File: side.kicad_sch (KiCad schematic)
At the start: 52 parts, among them SW1 SW_Push, SW11 SW_Push, SW12 SW_Push, SW13 SW_Push, SW14 SW_Push, SW15 SW_Push, SW21 SW_Push, SW22 SW_Push, SW23 SW_Push, SW24 SW_Push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

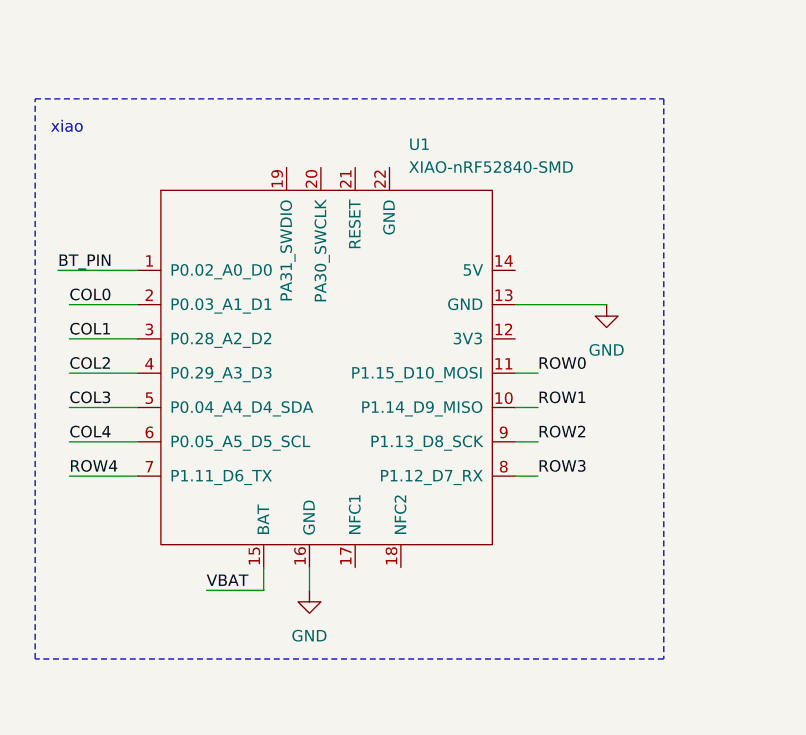
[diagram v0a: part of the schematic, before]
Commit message: Added links to parts
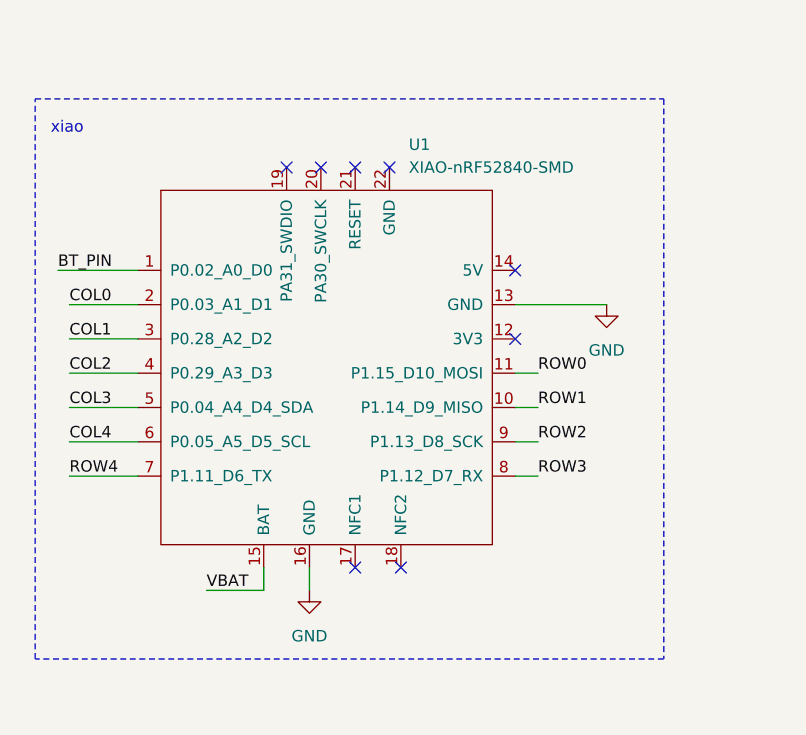
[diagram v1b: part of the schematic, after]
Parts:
- D1, D11, D12, D13, D14, D15, D21, D22, D23, D24, D25, D3, D31, D32, D33, D34, D35, D41, D5, D7, D9: footprint (none) -> Diode_SMD:D_SOD-123
- H1, H3, H5, H6, H9: footprint (none) -> Panelization:mouse-bite-5mm-slot
- R1, R3: footprint (none) -> Resistor_SMD:R_0805_2012Metric
- SW1, SW11, SW12, SW13, SW14, SW15, SW21, SW22, SW23, SW24, SW25, SW3, SW31, SW32, SW33, SW34, SW35, SW41, SW5, SW7, SW9: footprint (none) -> PCM_marbastlib-choc:SW_choc_v1_HS_CPG135001S30_1u
- TP1, TP3: footprint (none) -> TestPoint:TestPoint_Pad_D2.0mm
- U1: footprint (none) -> XIAO:modified-XIAO-nRF52840-SMD
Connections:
- no-connect marks 0 -> 8
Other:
- title: (none) -> Keyboard
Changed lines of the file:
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@@
 	(generator_version "9.0")
 	(paper "A4")
+	(title_block
+		(title "Keyboard")
+		(date "2026-04-17")
+		(comment 1 "Keyboard Schematic Editor")
+	)
 	(rectangle
 		(start 31.75 78.74)
@@
 		(color 0 0 0 0)
 	)
+	(no_connect
+		(at 67.31 86.36)
+	)
+	(no_connect
+		(at 85.09 105.41)
+	)
+	(no_connect
+		(at 85.09 97.79)
+	)
+	(no_connect
+		(at 63.5 86.36)
+	)
+	(no_connect
+		(at 59.69 86.36)
+	)
+	(no_connect
+		(at 67.31 130.81)
+	)
+	(no_connect
+		(at 72.39 130.81)
+	)
+	(no_connect
+		(at 71.12 86.36)
+	)
 	(wire
 		(pts
@@
 	(wire
 		(pts
+			(xy 85.09 101.6) (xy 95.25 101.6)
+		)
+		(stroke
+			(width 0)
+			(type default)
+		)
+	)
+	(wire
+		(pts
 			(xy 34.29 97.79) (xy 43.18 97.79)
 		)
@@
 	(wire
 		(pts
-			(xy 85.09 101.6) (xy 95.25 101.6)
-		)
-		(stroke
-			(width 0)
-			(type default)
-		)
-	)
-	(wire
-		(pts
 			(xy 234.95 97.79) (xy 234.95 115.57)
 		)
@@
 			)
 		)
-		(property "Footprint" ""
+		(property "Footprint" "PCM_marbastlib-choc:SW_choc_v1_HS_CPG135001S30_1u"
 			(at 207.01 110.49 0)
 			(effects
@@
 			)
 		)
-		(property "Footprint" ""
+		(property "Footprint" "PCM_marbastlib-choc:SW_choc_v1_HS_CPG135001S30_1u"
 			(at 223.52 110.49 0)
 			(effects
@@
 			)
 		)
-		(property "Footprint" ""
+		(property "Footprint" "PCM_marbastlib-choc:SW_choc_v1_HS_CPG135001S30_1u"
 			(at 173.99 74.93 0)
 			(effects
@@
 			)
 		)
-		(property "Footprint" ""
+		(property "Footprint" "Diode_SMD:D_SOD-123"
 			(at 195.58 119.38 0)
 			(effects
@@
 			)
 		)
-		(property "Footprint" ""
+		(property "Footprint" "PCM_marbastlib-choc:SW_choc_v1_HS_CPG135001S30_1u"
 			(at 207.01 57.15 0)
 			(effects
@@
 			)
 		)
-		(property "Footprint" ""
+		(property "Footprint" "PCM_marbastlib-choc:SW_choc_v1_HS_CPG135001S30_1u"
 			(at 240.03 74.93 0)
 			(effects
@@
 			)
 		)
-		(property "Footprint" ""
+		(property "Footprint" "PCM_marbastlib-choc:SW_choc_v1_HS_CPG135001S30_1u"
 			(at 223.52 57.15 0)
 			(effects
@@
 			)
 		)
-		(property "Footprint" ""
+		(property "Footprint" "PCM_marbastlib-choc:SW_choc_v1_HS_CPG135001S30_1u"
 			(at 223.52 92.71 0)
 			(effects
@@
 			)
 		)
-		(property "Footprint" ""
+		(property "Footprint" "Panelization:mouse-bite-5mm-slot"
 			(at 44.45 186.69 0)
 			(effects
@@
 			)
 		)
-		(property "Footprint" ""
+		(property "Footprint" "Diode_SMD:D_SOD-123"
 			(at 195.58 101.6 0)
 			(effects
@@
 			)
 		)
-		(property "Footprint" ""
+		(property "Footprint" "PCM_marbastlib-choc:SW_choc_v1_HS_CPG135001S30_1u"
 			(at 190.5 92.71 0)
 			(effects
@@
 			)
 		)
-		(property "Footprint" ""
+		(property "Footprint" "Diode_SMD:D_SOD-123"
 			(at 212.09 66.04 0)
 			(effects
@@
 			)
 		)
-		(property "Footprint" ""
+		(property "Footprint" "PCM_marbastlib-choc:SW_choc_v1_HS_CPG135001S30_1u"
 			(at 240.03 110.49 0)
 			(effects
@@
 			)
 		)
-		(property "Footprint" ""
+		(property "Footprint" "PCM_marbastlib-choc:SW_choc_v1_HS_CPG135001S30_1u"
 			(at 173.99 57.15 0)
 			(effects
@@
 			)
 		)
-		(property "Footprint" ""
+		(property "Footprint" "PCM_marbastlib-choc:SW_choc_v1_HS_CPG135001S30_1u"
 			(at 240.03 57.15 0)
 			(effects
@@
 			)
 		)
-		(property "Footprint" ""
+		(property "Footprint" "PCM_marbastlib-choc:SW_choc_v1_HS_CPG135001S30_1u"
 			(at 207.01 74.93 0)
 			(effects
@@
 			)
 		)
-		(property "Footprint" ""
+		(property "Footprint" "Resistor_SMD:R_0805_2012Metric"
 			(at 82.55 44.958 90)
 			(effects
@@
 			)
 		)
-		(property "Footprint" ""
+		(property "Footprint" "Diode_SMD:D_SOD-123"
 			(at 245.11 83.82 0)
 			(effects
@@
 			)
 		)
-		(property "Footprint" ""
+		(property "Footprint" "PCM_marbastlib-choc:SW_choc_v1_HS_CPG135001S30_1u"
 			(at 173.99 92.71 0)
 			(effects
@@
 			)
 		)
-		(property "Footprint" ""
+		(property "Footprint" "Diode_SMD:D_SOD-123"
 			(at 228.6 66.04 0)
 			(effects
@@
 			)
 		)
-		(property "Footprint" ""
+		(property "Footprint" "Diode_SMD:D_SOD-123"
 			(at 179.07 66.04 0)
 			(effects
@@
 			)
 		)
-		(property "Footprint" ""
+		(property "Footprint" "Diode_SMD:D_SOD-123"
 			(at 212.09 83.82 0)
 			(effects
@@
 			)
 		)
-		(property "Footprint" ""
+		(property "Footprint" "PCM_marbastlib-choc:SW_choc_v1_HS_CPG135001S30_1u"
 			(at 207.01 92.71 0)
 			(effects
@@
 			)
 		)
-		(property "Footprint" ""
+		(property "Footprint" "PCM_marbastlib-choc:SW_choc_v1_HS_CPG135001S30_1u"
 			(at 190.5 110.49 0)
 			(effects
@@
 			)
 		)
-		(property "Footprint" ""
+		(property "Footprint" "PCM_marbastlib-choc:SW_choc_v1_HS_CPG135001S30_1u"
 			(at 190.5 57.15 0)
 			(effects
@@
 			)
 		)
-		(property "Footprint" ""
+		(property "Footprint" "Resistor_SMD:R_0805_2012Metric"
 			(at 97.79 44.958 90)
 			(effects
@@
 			)
 		)
-		(property "Footprint" ""
+		(property "Footprint" "Diode_SMD:D_SOD-123"
 			(at 212.09 119.38 0)
 			(effects
@@
 			)
 		)
-		(property "Footprint" ""
+		(property "Footprint" "Panelization:mouse-bite-5mm-slot"
 			(at 53.34 186.69 0)
 			(effects
@@
 			)
 		)
-		(property "Footprint" ""
+		(property "Footprint" "TestPoint:TestPoint_Pad_D2.0mm"
 			(at 44.45 40.64 0)
 			(effects
@@
 			)
 		)
-		(property "Footprint" ""
+		(property "Footprint" "Diode_SMD:D_SOD-123"
 			(at 179.07 83.82 0)
 			(effects
@@
 			)
 		)
-		(property "Footprint" ""
+		(property "Footprint" "PCM_marbastlib-choc:SW_choc_v1_HS_CPG135001S30_1u"
 			(at 240.03 92.71 0)
 			(effects
@@
 			)
 		)
-		(property "Footprint" ""
+		(property "Footprint" "Diode_SMD:D_SOD-123"
 			(at 212.09 101.6 0)
 			(effects
@@
 			)
 		)
-		(property "Footprint" ""
+		(property "Footprint" "Diode_SMD:D_SOD-123"
 			(at 245.11 119.38 0)
 			(effects
@@
 			)
 		)
-		(property "Footprint" ""
+		(property "Footprint" "Diode_SMD:D_SOD-123"
 			(at 245.11 101.6 0)
 			(effects
@@
 			)
 		)
-		(property "Footprint" ""
+		(property "Footprint" "Diode_SMD:D_SOD-123"
 			(at 228.6 101.6 0)
 			(effects
@@
 			)
 		)
-		(property "Footprint" ""
+		(property "Footprint" "Diode_SMD:D_SOD-123"
 			(at 179.07 101.6 0)
 			(effects
@@
 			)
 		)
-		(property "Footprint" ""
+		(property "Footprint" "Diode_SMD:D_SOD-123"
 			(at 228.6 83.82 0)
 			(effects
@@
 			)
 		)
-		(property "Footprint" ""
+		(property "Footprint" "Diode_SMD:D_SOD-123"
 			(at 245.11 137.16 0)
 			(effects
@@
 			)
 		)
-		(property "Footprint" ""
+		(property "Footprint" "PCM_marbastlib-choc:SW_choc_v1_HS_CPG135001S30_1u"
 			(at 240.03 128.27 0)
 			(effects
@@
 			)
 		)
-		(property "Footprint" ""
+		(property "Footprint" "PCM_marbastlib-choc:SW_choc_v1_HS_CPG135001S30_1u"
 			(at 190.5 74.93 0)
 			(effects
@@
 			)
 		)
-		(property "Footprint" ""
+		(property "Footprint" "Diode_SMD:D_SOD-123"
 			(at 179.07 119.38 0)
 			(effects
@@
 			)
 		)
-		(property "Footprint" ""
+		(property "Footprint" "XIAO:modified-XIAO-nRF52840-SMD"
 			(at 55.88 104.14 0)
 			(effects
@@
 			)
 		)
-		(property "Footprint" ""
+		(property "Footprint" "PCM_marbastlib-choc:SW_choc_v1_HS_CPG135001S30_1u"
 			(at 223.52 74.93 0)
 			(effects
@@
 			)
 		)
-		(property "Footprint" ""
+		(property "Footprint" "Diode_SMD:D_SOD-123"
 			(at 195.58 83.82 0)
 			(effects
@@
 			)
 		)
-		(property "Footprint" ""
+		(property "Footprint" "Diode_SMD:D_SOD-123"
 			(at 228.6 119.38 0)
 			(effects
@@
 			)
 		)
-		(property "Footprint" ""
+		(property "Footprint" "TestPoint:TestPoint_Pad_D2.0mm"
 			(at 44.45 30.48 0)
 			(effects
@@
 			)
 		)
-		(property "Footprint" ""
+		(property "Footprint" "Panelization:mouse-bite-5mm-slot"
 			(at 71.12 186.69 0)
 			(effects
@@
 			)
 		)
-		(property "Footprint" ""
+		(property "Footprint" "Panelization:mouse-bite-5mm-slot"
 			(at 62.23 186.69 0)
 			(effects
@@
 			)
 		)
-		(property "Footprint" ""
+		(property "Footprint" "Diode_SMD:D_SOD-123"
 			(at 245.11 66.04 0)
 			(effects
@@
 			)
 		)
-		(property "Footprint" ""
+		(property "Footprint" "Diode_SMD:D_SOD-123"
 			(at 195.58 66.04 0)
 			(effects
@@
 			)
 		)
-		(property "Footprint" ""
+		(property "Footprint" "Panelization:mouse-bite-5mm-slot"
 			(at 35.56 186.69 0)
 			(effects
@@
 			)
 		)
-		(property "Footprint" ""
+		(property "Footprint" "PCM_marbastlib-choc:SW_choc_v1_HS_CPG135001S30_1u"
 			(at 173.99 110.49 0)
 			(effects

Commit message: Changed keyboard layout to 4*13
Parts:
- removed D41: D, Diode_SMD:D_SOD-123, symbol Device:D
- removed SW41: SW_Push, PCM_marbastlib-choc:SW_choc_v1_HS_CPG135001S30_1u, symbol Switch:SW_Push
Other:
- moved on the sheet: D1, D11, D12, D13, D14, D15, D21, D22, D23, D24, D25, D3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
